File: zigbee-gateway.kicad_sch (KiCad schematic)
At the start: 13 parts, among them J1 Conn_01x04, J2 Conn_01x04, SW1 SW_Push, SW2 SW_Push, SW3 SW_Push, U1 ESP-12E, U2 CC2530-A1_Module

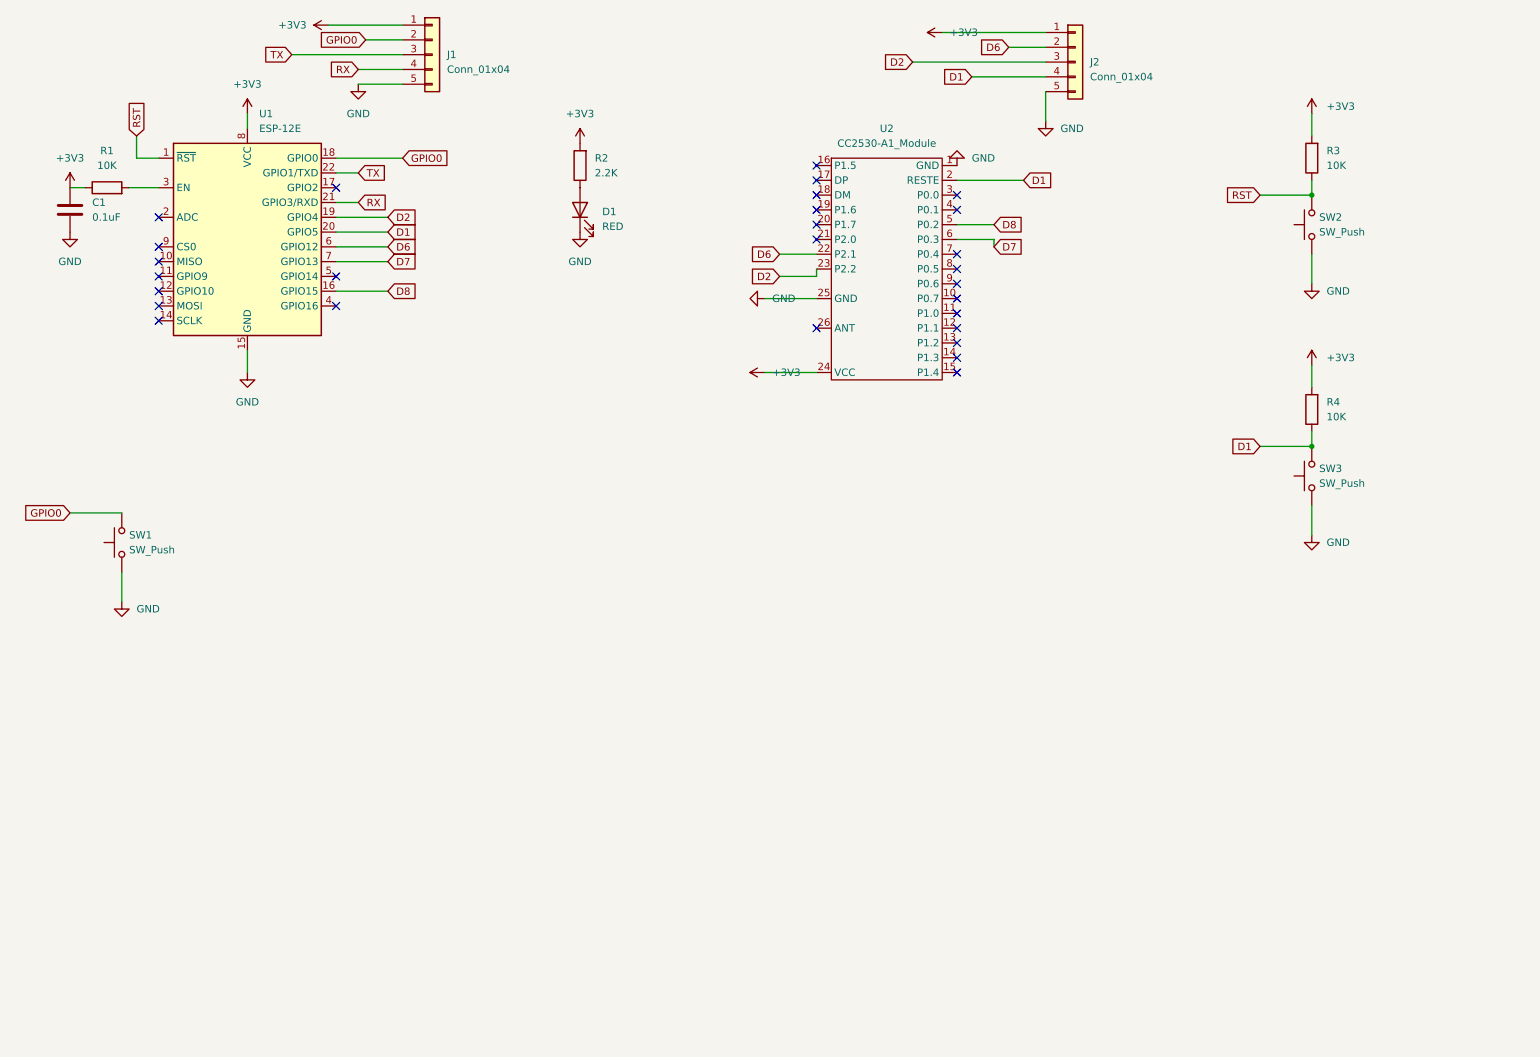
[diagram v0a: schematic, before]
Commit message: ome changes performed for adding switching to the board
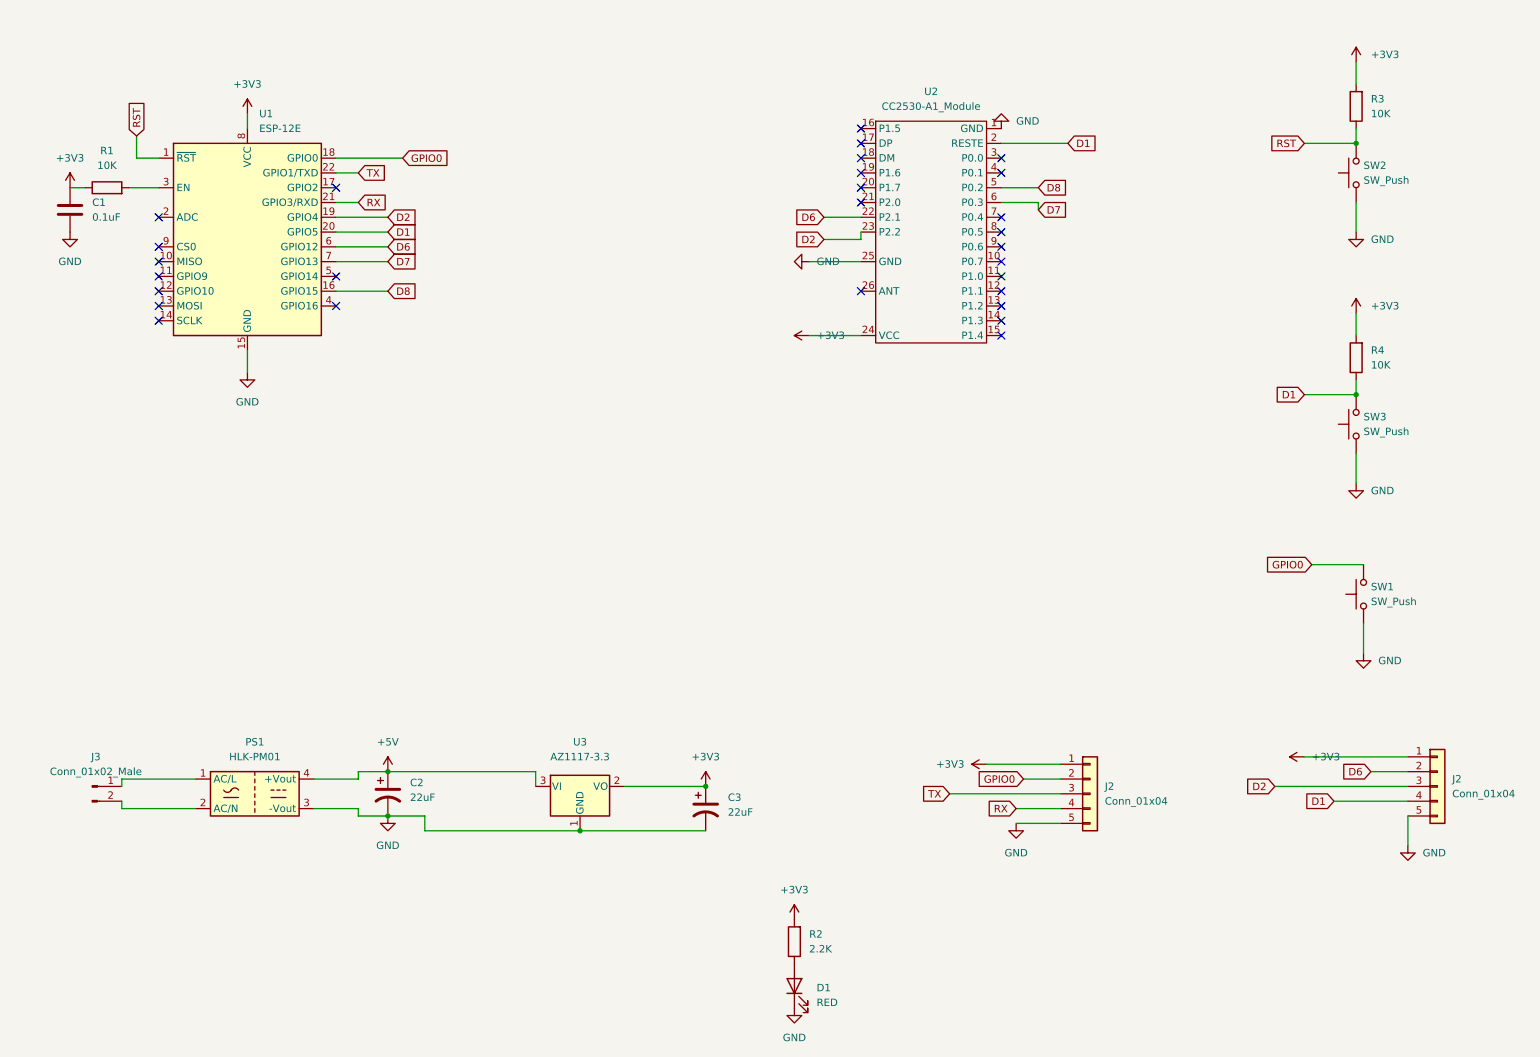
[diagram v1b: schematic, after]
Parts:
- removed J1, J2: Conn_01x04, Connector_PinHeader_2.54mm:PinHeader_1x05_P2.54mm_Horizontal, symbol Connector_Generic:Conn_01x05
- added C2, C3: 22uF, Capacitor_Tantalum_SMD:CP_EIA-1608-10_AVX-L_Pad1.25x1.05mm_HandSolder, symbol Device:C_Polarized_US
- added J2 (x2): Conn_01x04, Connector_PinHeader_2.54mm:PinHeader_1x05_P2.54mm_Vertical, symbol Connector_Generic:Conn_01x05
- added J3: Conn_01x02_Male, Connector_Pin:Pin_D1.4mm_L8.5mm_W2.8mm_FlatFork, symbol Connector:Conn_01x02_Male
- added PS1: HLK-PM01, Converter_ACDC:Converter_ACDC_HiLink_HLK-PMxx, symbol Converter_ACDC:HLK-PM01
- added U3: AZ1117-3.3, Package_TO_SOT_SMD:SOT-223-3_TabPin2, symbol Regulator_Linear:AZ1117-3.3
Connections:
- net +3V3: now also C3.1, J2.1 (Pin_1), J2.1 (Pin_1), U3.2 (VO)
- net D1: now also J2.4 (Pin_4)
- net D2: now also J2.3 (Pin_3)
- net D6: now also J2.2 (Pin_2)
- net GND: now also C2.2, C3.2, J2.5 (Pin_5), J2.5 (Pin_5), PS1.3 (-Vout), U3.1 (GND)
- net GPIO0: now also J2.2 (Pin_2)
- net RX: now also J2.4 (Pin_4)
- net TX: now also J2.3 (Pin_3)
- new net: J3.1 (Pin_1), PS1.1 (AC/L)
- new net: J3.2 (Pin_2), PS1.2 (AC/N)
- new net +5V: C2.1, PS1.4 (+Vout), U3.3 (VI)
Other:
- moved on the sheet: D1, R2, R3, R4, SW1, SW2, SW3, U2
